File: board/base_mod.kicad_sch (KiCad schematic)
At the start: 19 parts, among them J11 RS-232, Q5 BC548, Q6 BC548, U4 AT24C1024B, U5 MAX3232, U6 24LCxxx

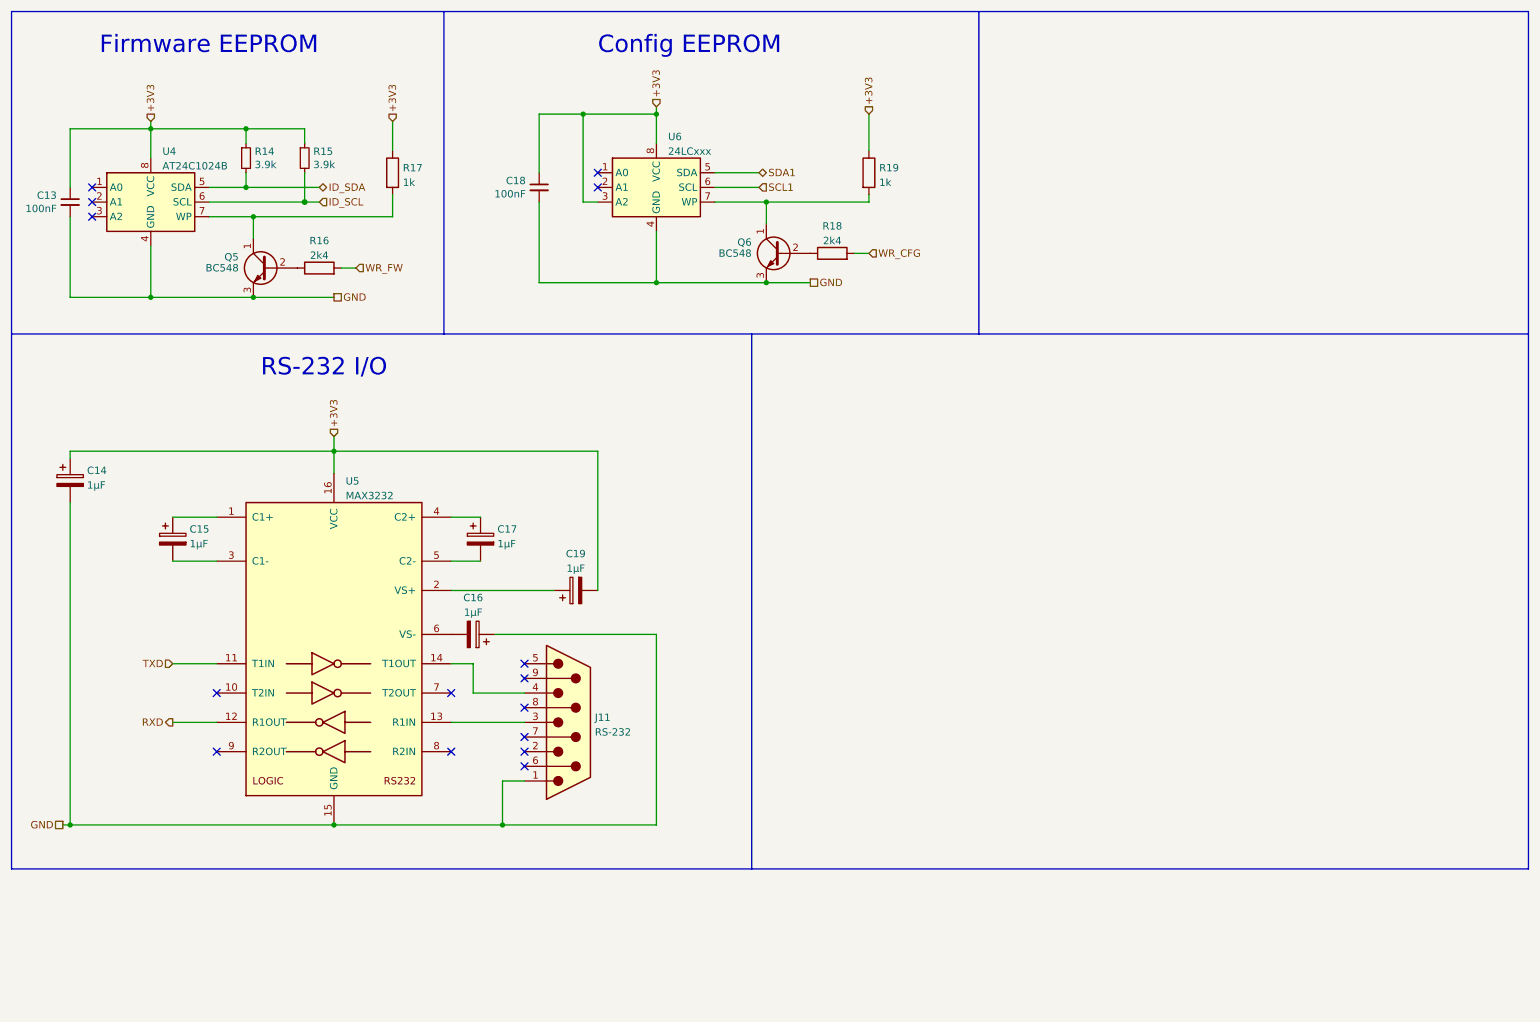
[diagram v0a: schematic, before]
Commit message: Modularize board.
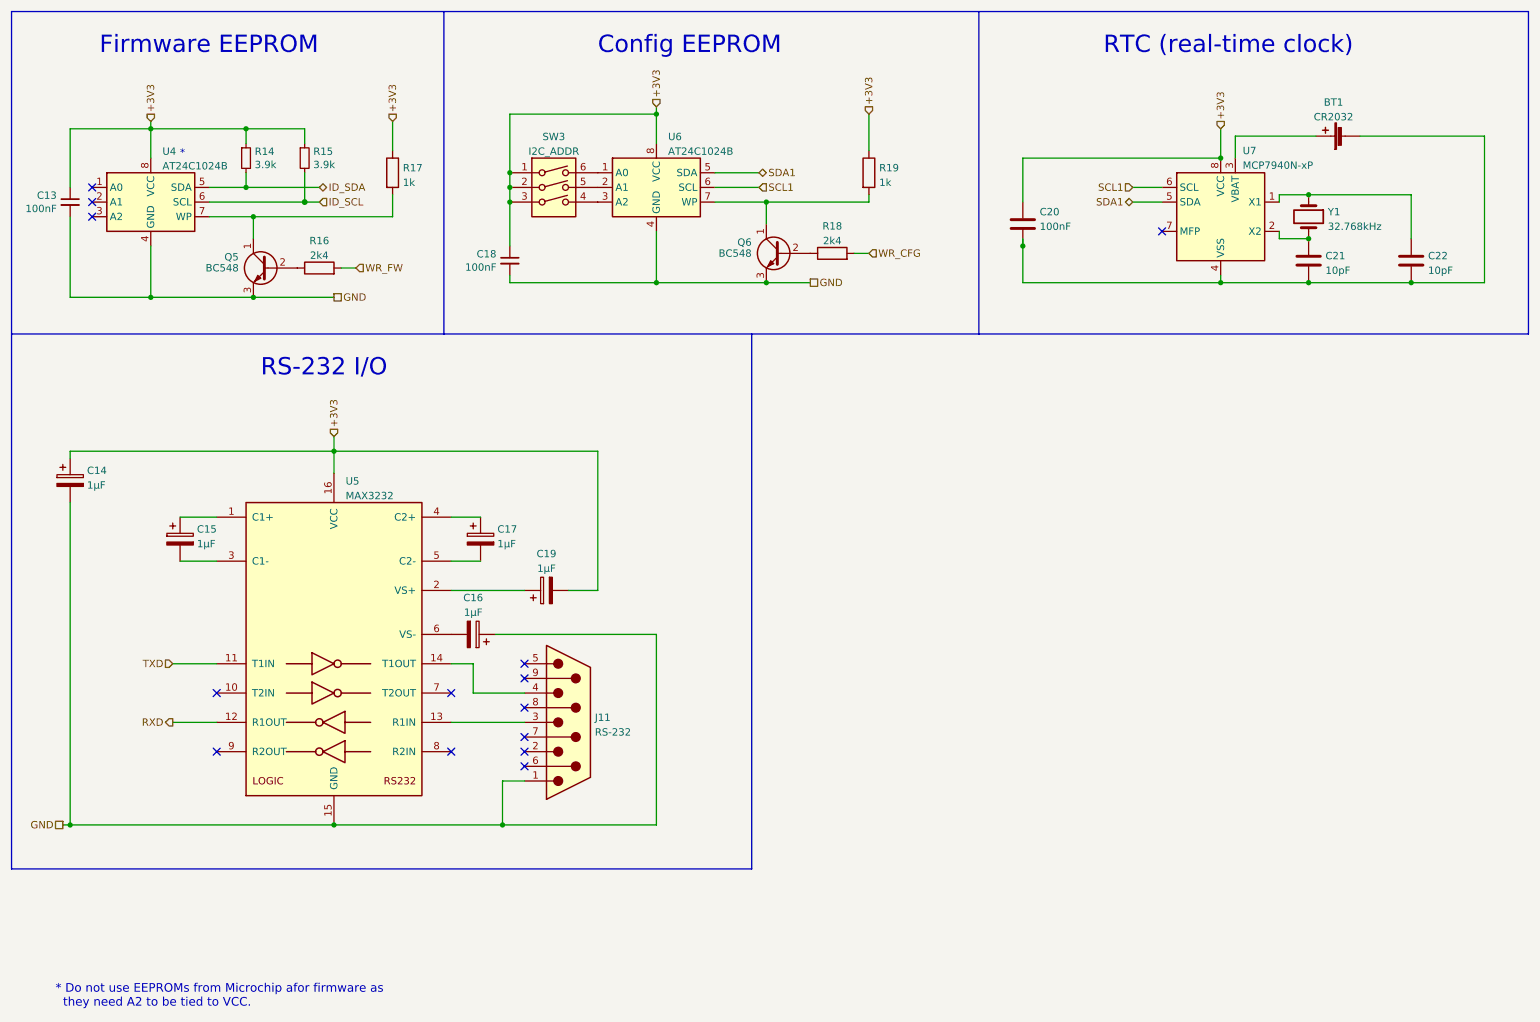
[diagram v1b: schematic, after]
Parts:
- removed U6: 24LCxxx, Package_DIP:DIP-8_W7.62mm_Socket_LongPads, symbol Memory_EEPROM:24LC1025
- added BT1: CR2032, Battery:Battery_Panasonic_CR2032-VS1N_Vertical_CircularHoles, symbol Device:Battery_Cell
- added C20: 100nF, Capacitor_THT:C_Disc_D5.0mm_W2.5mm_P5.00mm, symbol Device:C
- added C21, C22: 10pF, Capacitor_THT:C_Radial_D6.3mm_H5.0mm_P2.50mm, symbol Device:C
- added SW3: I2C_ADDR, Button_Switch_THT:SW_DIP_SPSTx03_Slide_9.78x9.8mm_W7.62mm_P2.54mm, symbol Switch:SW_DIP_x03
- added U6: AT24C1024B, Package_DIP:DIP-8_W7.62mm_LongPads, symbol Memory_EEPROM:CAT24C128
- added U7: MCP7940N-xP, Package_DIP:DIP-8_W7.62mm_Socket_LongPads, symbol Timer_RTC:MCP7940N-xP
- added Y1: 32.768kHz, Crystal:Crystal_C26-LF_D2.1mm_L6.5mm_Vertical, symbol Device:Crystal
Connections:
- net +3V3: now also C20.1, SW3.1, SW3.2, SW3.3, U6.8 (VCC), U7.8 (VCC)
- net GND: now also U6.4 (GND)
- net SCL1: now also U6.6 (SCL), U7.6 (SCL)
- net SDA1: now also U6.5 (SDA), U7.5 (SDA)
- net at Q6.1 (C), R19.2: now also U6.7 (WP)
- new net: BT1.2 (-), C20.2, C21.2, C22.2, U7.4 (VSS)
- new net: SW3.6, U6.1 (A0)
- new net: SW3.5, U6.2 (A1)
- new net: SW3.4, U6.3 (A2)
- new net: C22.1, U7.1 (X1), Y1.1
- new net: C21.1, U7.2 (X2), Y1.2
- new net: BT1.1 (+), U7.3 (VBAT)
- no-connect marks 15 -> 14
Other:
- note added: "*"
- note added: "* Do not use EEPROMs from Microchip afor firmware as they need A2 to be tied to VCC."
- note added: "RTC (real-time clock)"
- moved on the sheet: C15, C18, C19
